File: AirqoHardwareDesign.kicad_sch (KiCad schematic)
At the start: 3 parts

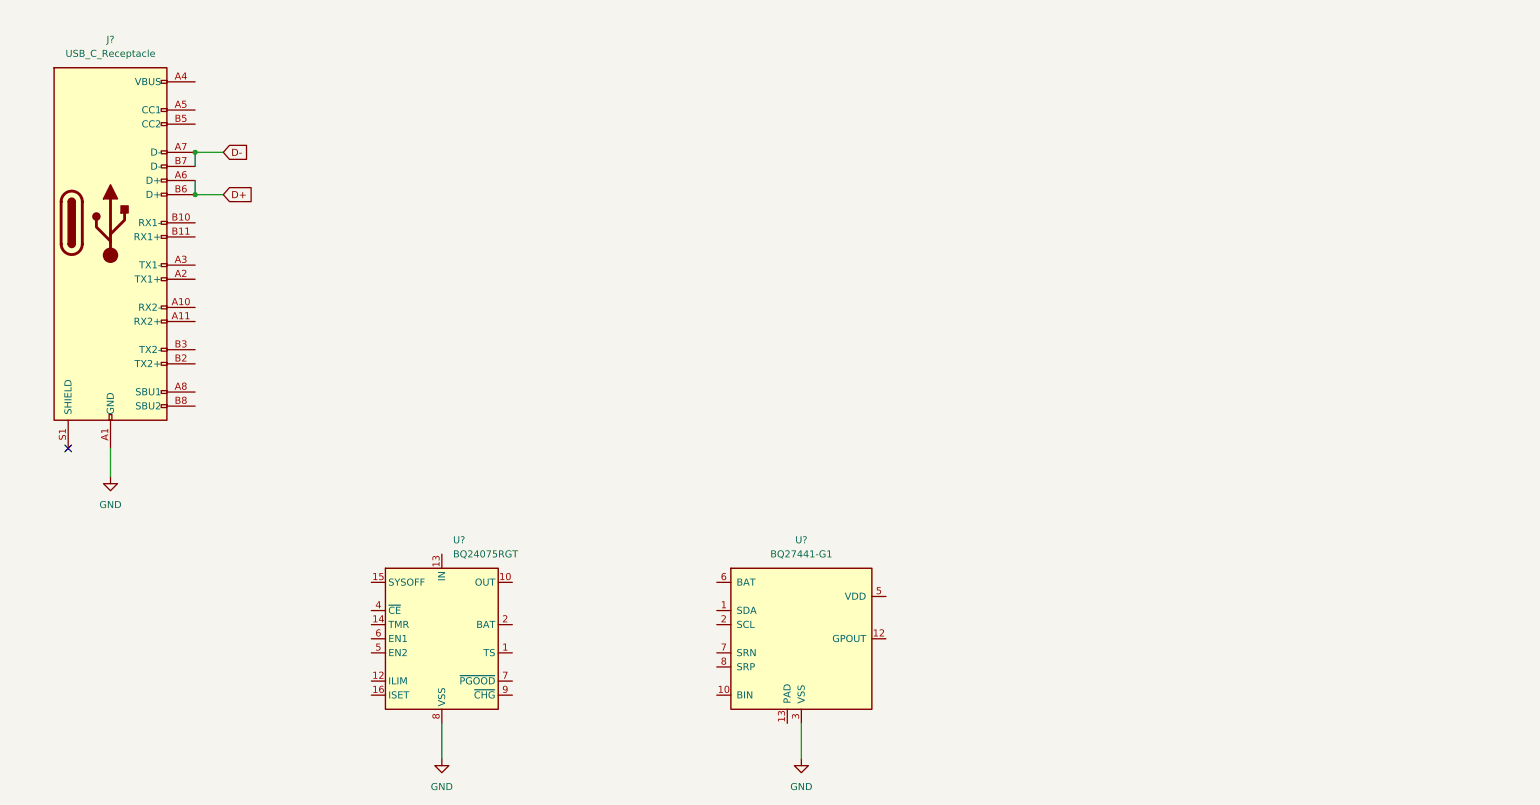
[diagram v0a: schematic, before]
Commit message: added passive componets to primary ICs
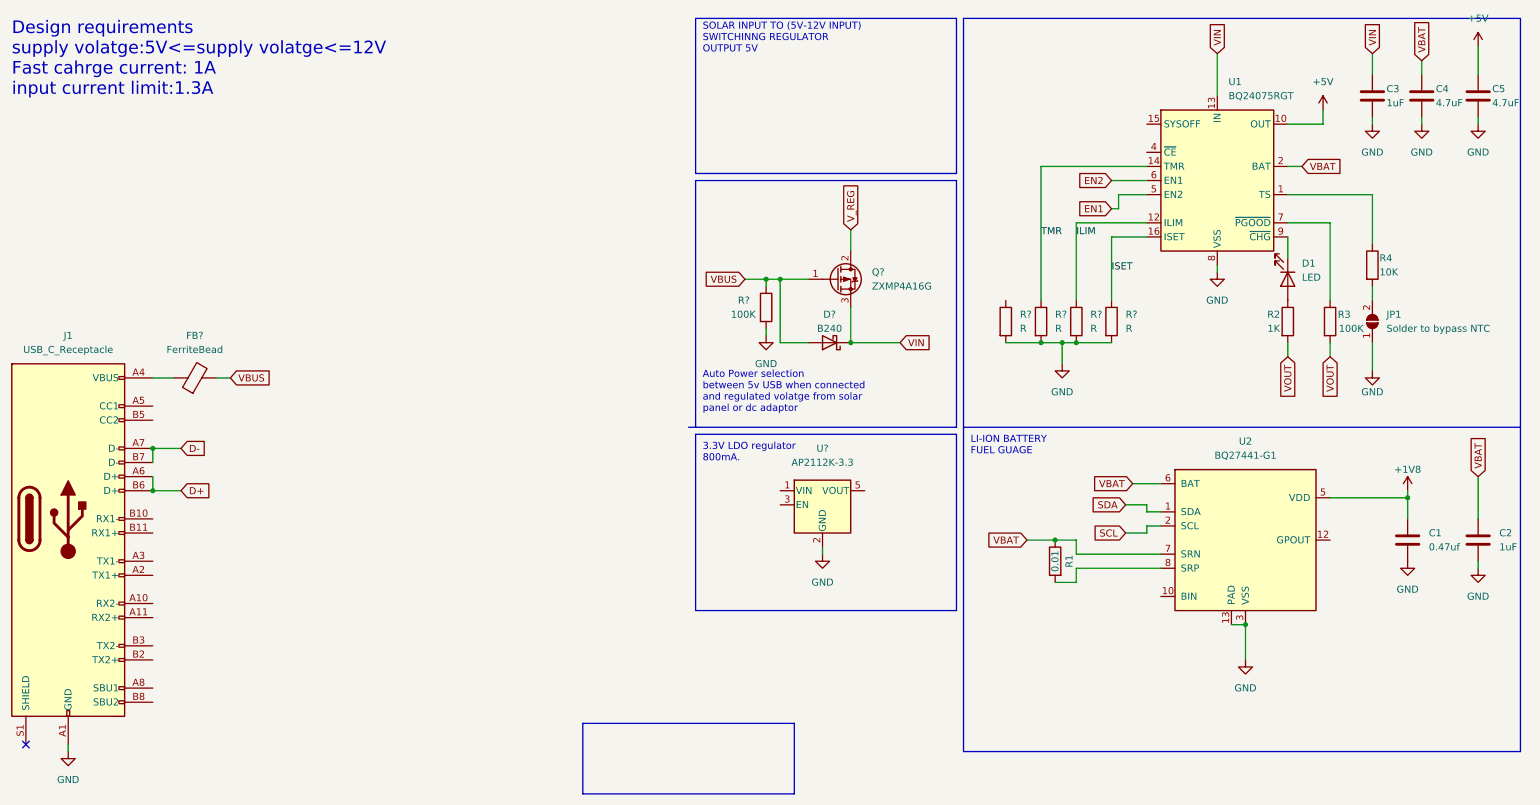
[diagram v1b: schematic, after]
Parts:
- added C1: 0.47uf, Capacitor_SMD:C_0603_1608Metric, symbol Device:C
- added C2: 1uF, Capacitor_SMD:C_0603_1608Metric, symbol Device:C
- added C3: 1uF, symbol Device:C
- added C4, C5: 4.7uF, symbol Device:C
- added D1: LED, symbol Device:LED
- added D?: B240, Diode_SMD:D_SMB, symbol Diode:B240
- added FB?: FerriteBead, symbol Device:FerriteBead
- added JP1: Solder to bypass NTC, symbol Jumper:SolderJumper_2_Open
- added Q?: ZXMP4A16G, Package_TO_SOT_SMD:SOT-223-3_TabPin2, symbol Transistor_FET:ZXMP4A16G
- added R1: 0.01, symbol Device:R
- added R2: 1K, symbol Device:R
- added R3, R?: 100K, symbol Device:R
- added R4: 10K, symbol Device:R
- added R? (x4): R, symbol Device:R
- added U?: AP2112K-3.3, Package_TO_SOT_SMD:SOT-23-5, symbol Regulator_Linear:AP2112K-3.3
- J1: renamed from J?; footprint (none) -> Connector_USB:USB_C_Receptacle_Amphenol_12401548E4-2A
- gave numbers to parts that had none: 2
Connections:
- net GND: now also U2.13 (PAD), C1.2, C2.2, C3.2, C4.2, C5.2, JP1.1 (A), R?.2, R?.2, R?.2, R?.2, R?.2, U?.2 (GND)
- net at U1.1 (TS): now also R4.1
- net +5V: now reaches U1.10 (OUT), U1.11 (OUT)
- net +5V: now also C5.1
- net ILIM: now reaches U1.12 (ILIM)
- net ILIM: now also R?.1
- net VIN: now reaches U1.13 (IN)
- net VIN: now also C3.1, D?.1 (K), Q?.3 (S)
- net TMR: now reaches U1.14 (TMR)
- net TMR: now also R?.1
- net ISET: now reaches U1.16 (ISET)
- net ISET: now also R?.1
- net VBAT: now reaches U1.2 (BAT), U1.3 (BAT)
- net VBAT: now also U2.6 (BAT), U2.7 (SRN), C2.1, C4.1, R1.1
- net EN1: now reaches U1.5 (EN2)
- net EN2: now reaches U1.6 (EN1)
- net at U1.7 (~{PGOOD}): now also R3.1
- net at U1.9 (~{CHG}): now also D1.1 (K)
- net SDA: now reaches U2.1 (SDA)
- net SCL: now reaches U2.2 (SCL)
- net +1V8: now reaches U2.5 (VDD)
- net +1V8: now also C1.1
- net at U2.8 (SRP): now also R1.2
- net at J1.A4 (VBUS), J1.A9 (VBUS), J1.B4 (VBUS)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: now also FB?.1
- new net: JP1.2 (B), R4.2
- new net: D1.2 (A), R2.1
- new net VBUS: D?.2 (A), FB?.2, Q?.1 (G), R?.1
- new net VOUT: R2.2, R3.2
- new net V_REG: Q?.2 (D)
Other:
- note added: "3.3V LDO regulator 800mA."
- note added: "Auto Power selection between 5v USB when connected and regulated volatge from solar panel or dc adaptor"
- note added: "Design requirements supply volatge:5V<=supply volatge<=12V Fast cahrge current: 1A input current limit:1.3A"
- note added: "LI-ION BATTERY FUEL GUAGE"
- note added: "SOLAR INPUT TO (5V-12V INPUT) SWITCHINNG REGULATOR OUTPUT 5V"
- moved on the sheet: J1, U1, U2
